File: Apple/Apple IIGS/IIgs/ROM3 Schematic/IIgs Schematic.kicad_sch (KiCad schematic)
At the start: 0 parts

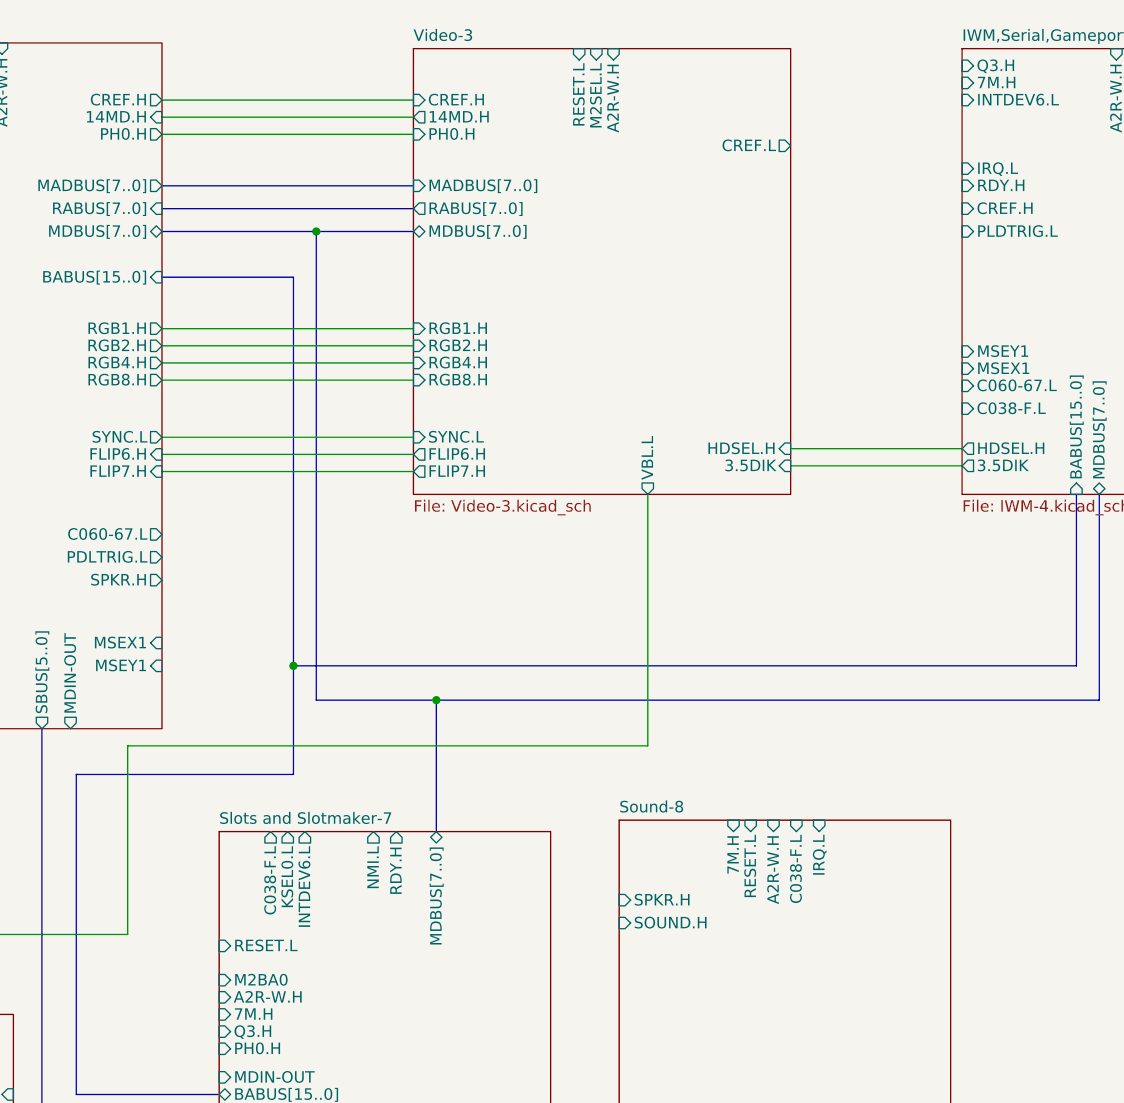
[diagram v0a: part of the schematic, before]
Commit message: 399 ERC, Rescue symbol clean-up
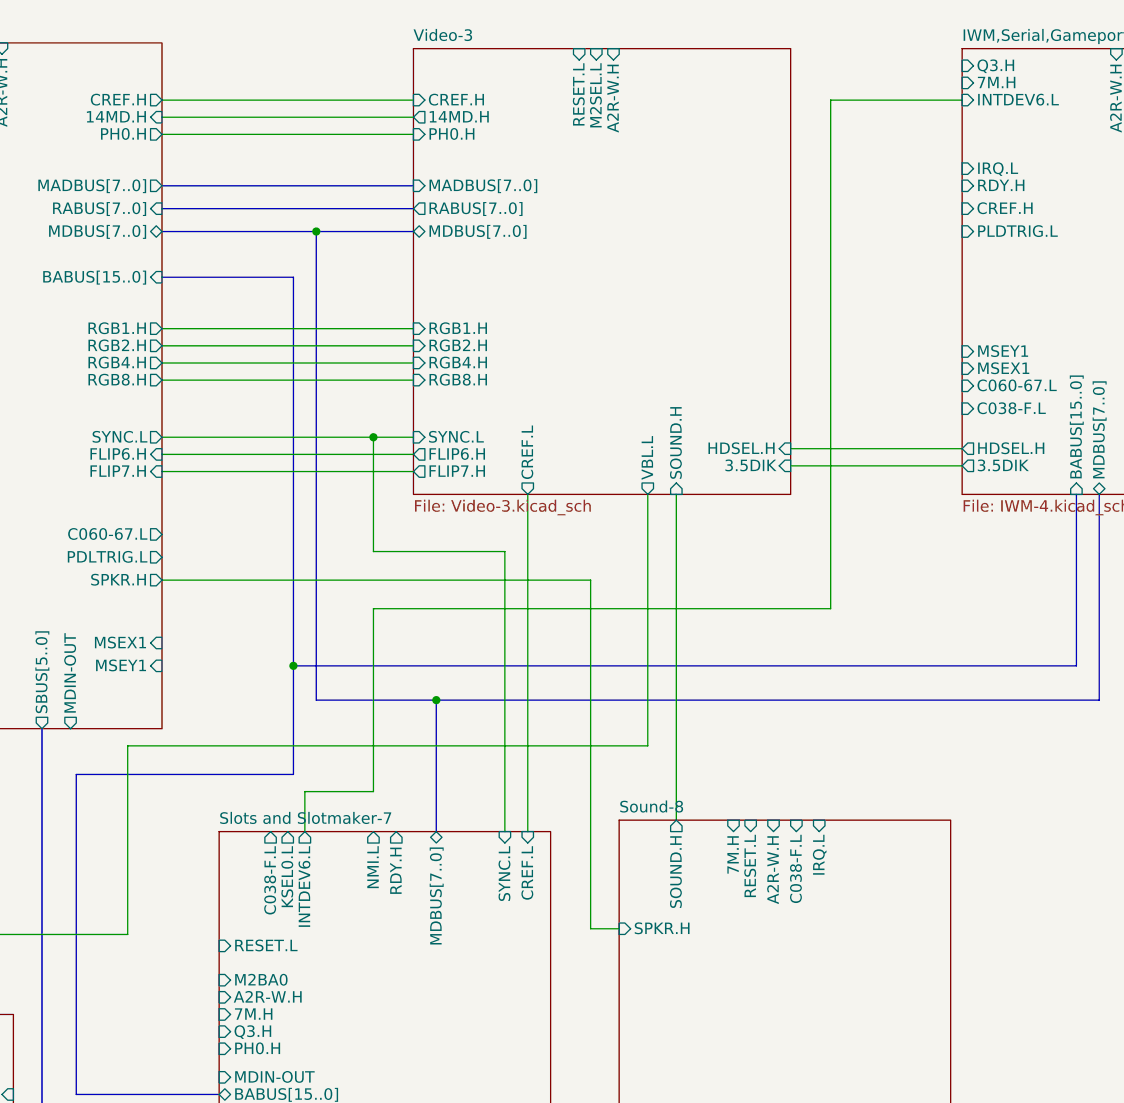
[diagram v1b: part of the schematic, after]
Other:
- sheet Slots and Slotmaker-7 ports: added CREF.L, SYNC.L; removed none
- sheet Video-3 ports: added SOUND.H; removed none

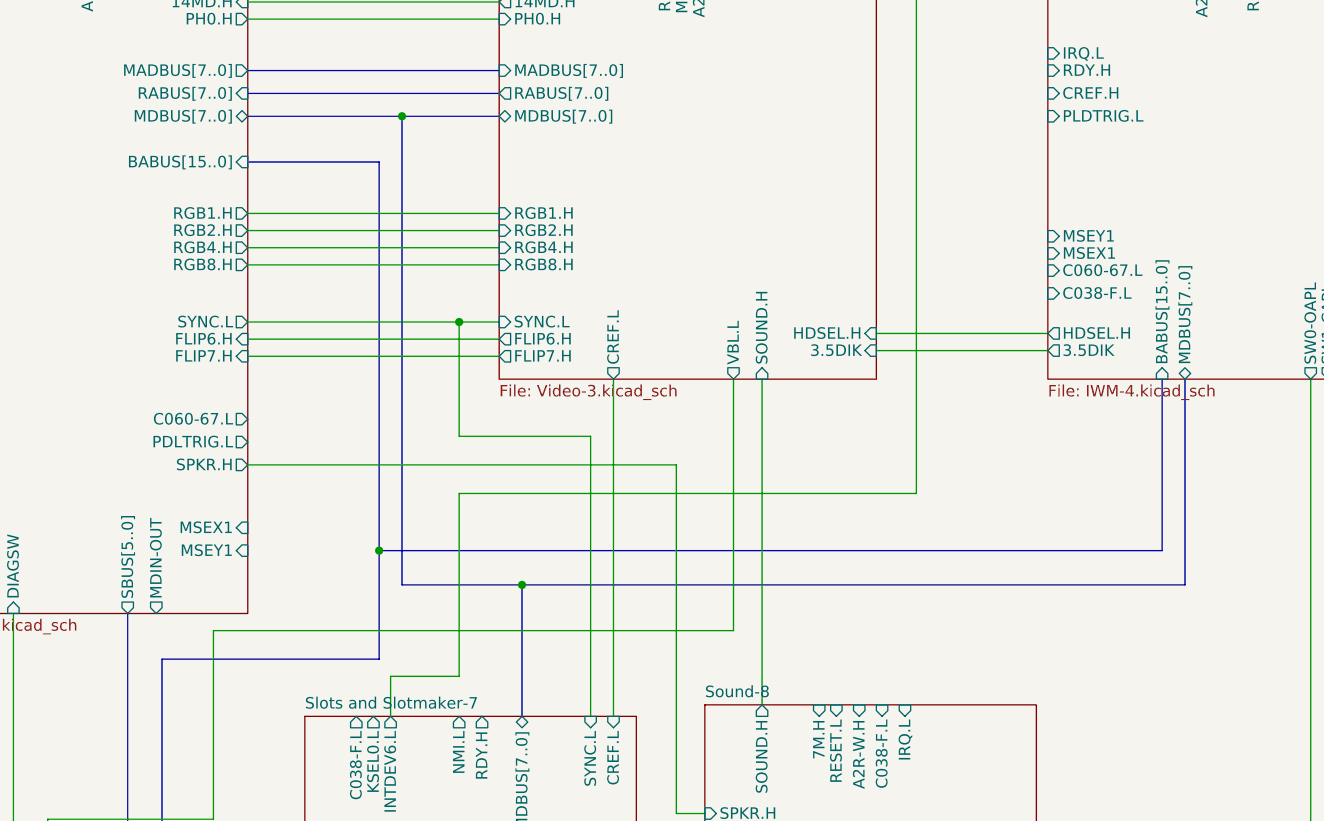
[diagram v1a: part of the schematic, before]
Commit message: moved v5 version to separate directory
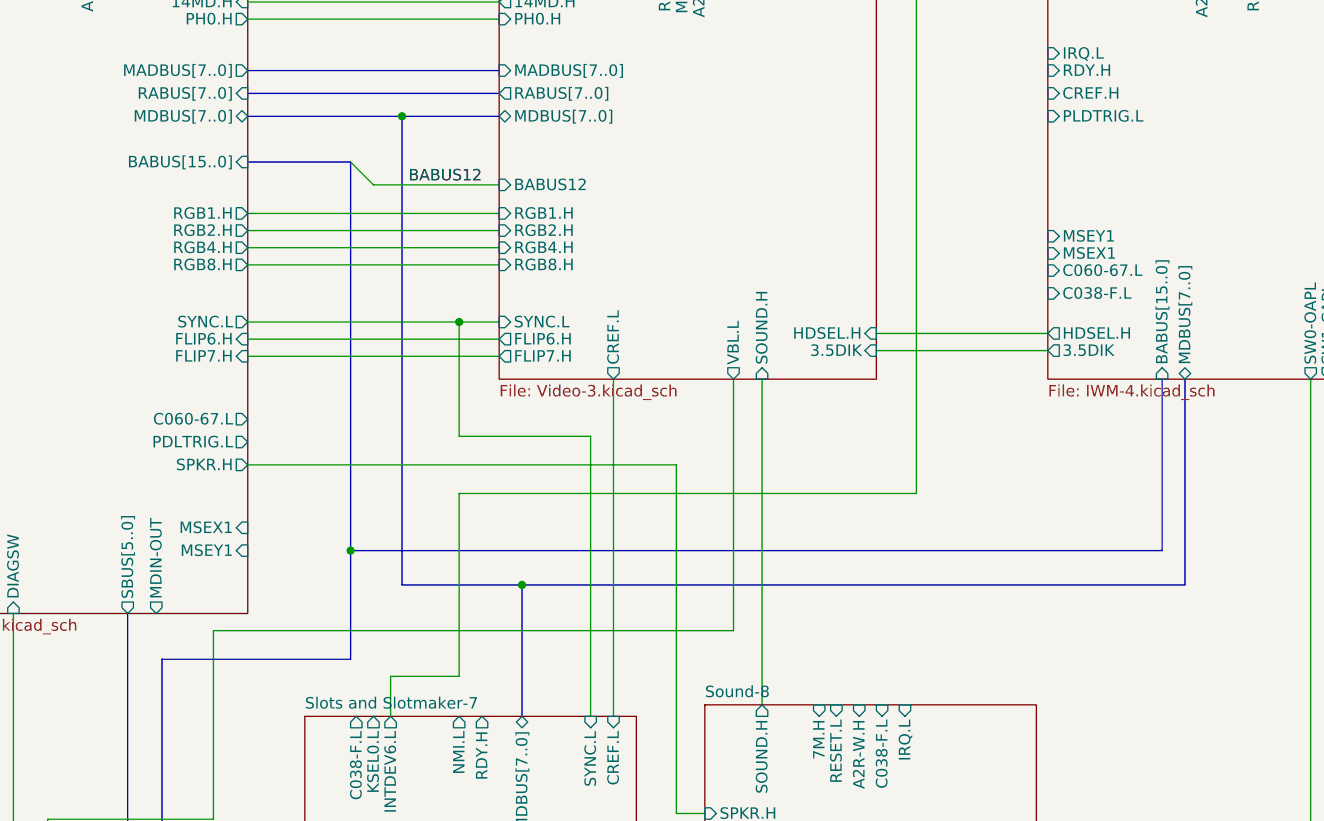
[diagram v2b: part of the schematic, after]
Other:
- sheet Video-3 ports: added BABUS12; removed none
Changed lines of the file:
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@@
   (junction (at 220.98 91.44) (diameter 0) (color 0 0 0 0)
   )
-  (junction (at 212.09 116.84) (diameter 0) (color 0 0 0 0)
+  (junction (at 208.915 116.84) (diameter 0) (color 0 0 0 0)
   )
   (junction (at 332.74 55.245) (diameter 0) (color 0 0 0 0)
   )
+  (bus_entry (at 208.915 73.66) (size 2.54 2.54)
+    (stroke (width 0) (type default) (color 0 0 0 0))
+  )
   (bus (pts (xy 214.63 68.58) (xy 225.425 68.58))
     (stroke (width 0) (type default) (color 0 0 0 0))
@@
     (stroke (width 0) (type default) (color 0 0 0 0))
   )
-  (bus (pts (xy 187.96 128.905) (xy 212.09 128.905))
+  (bus (pts (xy 208.915 116.84) (xy 299.085 116.84))
+    (stroke (width 0) (type default) (color 0 0 0 0))
+  )
+  (bus (pts (xy 187.96 128.905) (xy 208.915 128.905))
     (stroke (width 0) (type default) (color 0 0 0 0))
   )
@@
     (stroke (width 0) (type default) (color 0 0 0 0))
   )
+  (wire (pts (xy 211.455 76.2) (xy 225.425 76.2))
+    (stroke (width 0) (type default) (color 0 0 0 0))
+  )
   (bus (pts (xy 184.15 166.37) (xy 203.835 166.37))
     (stroke (width 0) (type default) (color 0 0 0 0))
@@
     (stroke (width 0) (type default) (color 0 0 0 0))
   )
-  (bus (pts (xy 212.09 116.84) (xy 212.09 128.905))
+  (bus (pts (xy 208.915 116.84) (xy 208.915 128.905))
     (stroke (width 0) (type default) (color 0 0 0 0))
   )
@@
     (stroke (width 0) (type default) (color 0 0 0 0))
   )
-  (bus (pts (xy 212.09 73.66) (xy 212.09 116.84))
+  (bus (pts (xy 208.915 73.66) (xy 208.915 116.84))
     (stroke (width 0) (type default) (color 0 0 0 0))
   )
@@
     (stroke (width 0) (type default) (color 0 0 0 0))
   )
-  (bus (pts (xy 212.09 116.84) (xy 299.085 116.84))
-    (stroke (width 0) (type default) (color 0 0 0 0))
-  )
   (wire (pts (xy 335.28 210.82) (xy 180.975 210.82))
     (stroke (width 0) (type default) (color 0 0 0 0))
@@
     (stroke (width 0) (type default) (color 0 0 0 0))
   )
-  (bus (pts (xy 197.485 73.66) (xy 212.09 73.66))
+  (bus (pts (xy 197.485 73.66) (xy 208.915 73.66))
     (stroke (width 0) (type default) (color 0 0 0 0))
   )
@@
   (bus (pts (xy 299.085 116.84) (xy 299.085 97.79))
     (stroke (width 0) (type default) (color 0 0 0 0))
+  )
+  (label "BABUS12" (at 223.52 76.2 180)
+    (effects (font (size 1.27 1.27)) (justify right bottom))
   )
   (sheet (at 88.265 47.625) (size 46.355 53.34) (fields_autoplaced)
@@
       (effects (font (size 1.27 1.27)) (justify left))
     )
+    (pin "BABUS12" input (at 225.425 76.2 180)
+      (effects (font (size 1.27 1.27)) (justify left))
+    )

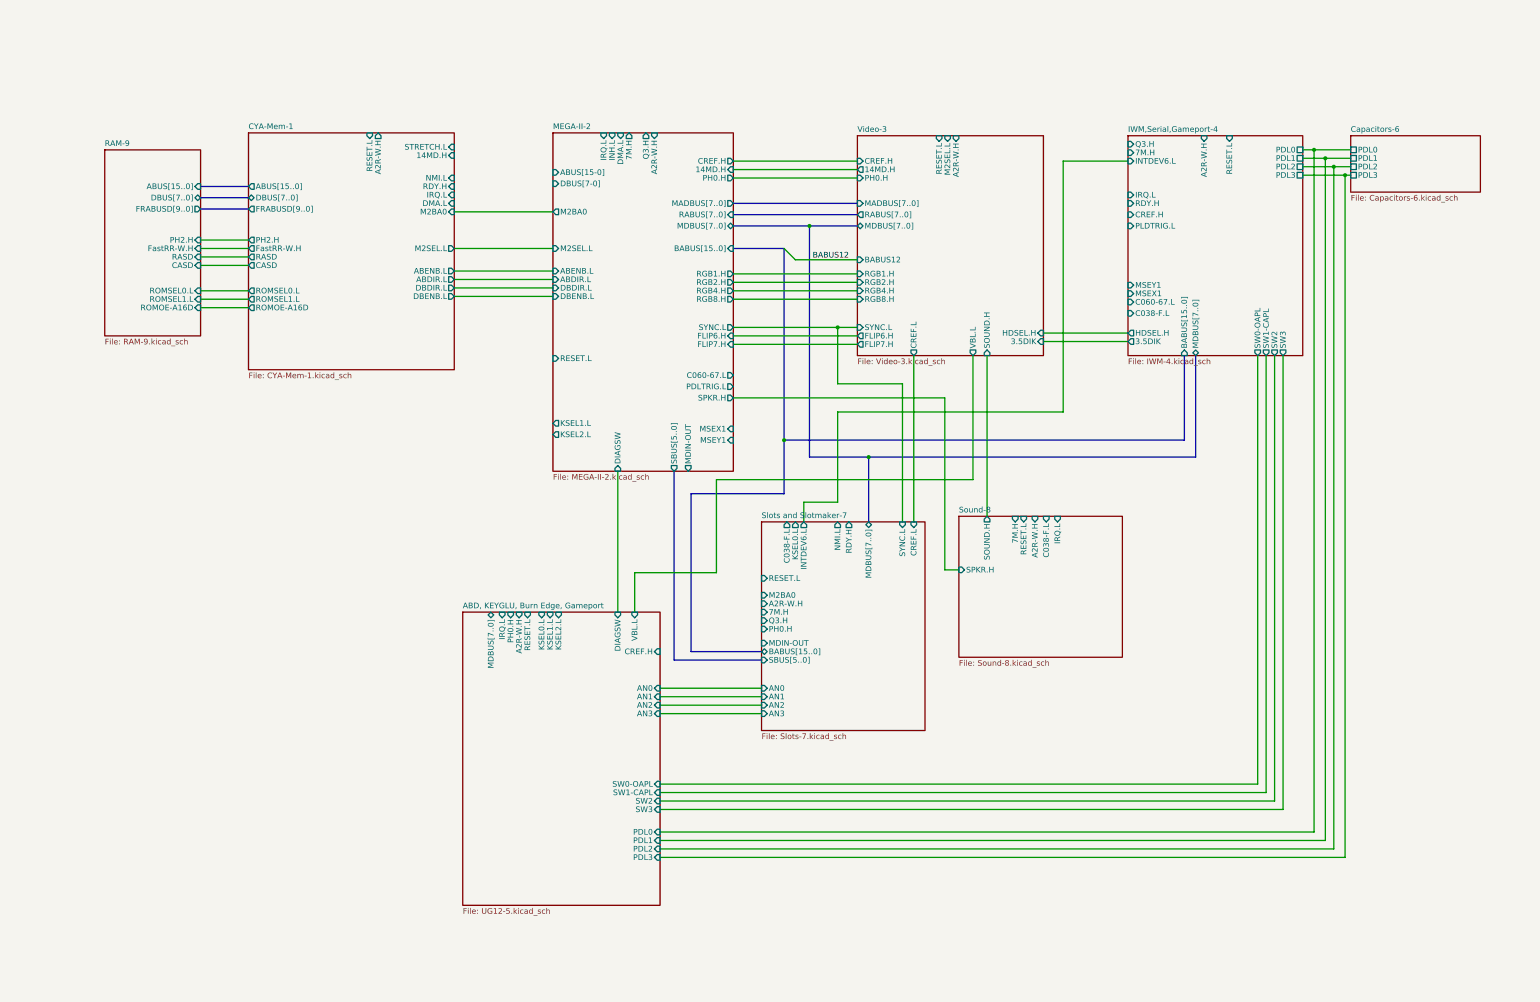
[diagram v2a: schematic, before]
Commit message: 0 ERC Errors AND Warnings. Whew. ICs updated with correct pin assignments and many (many) other fixes.
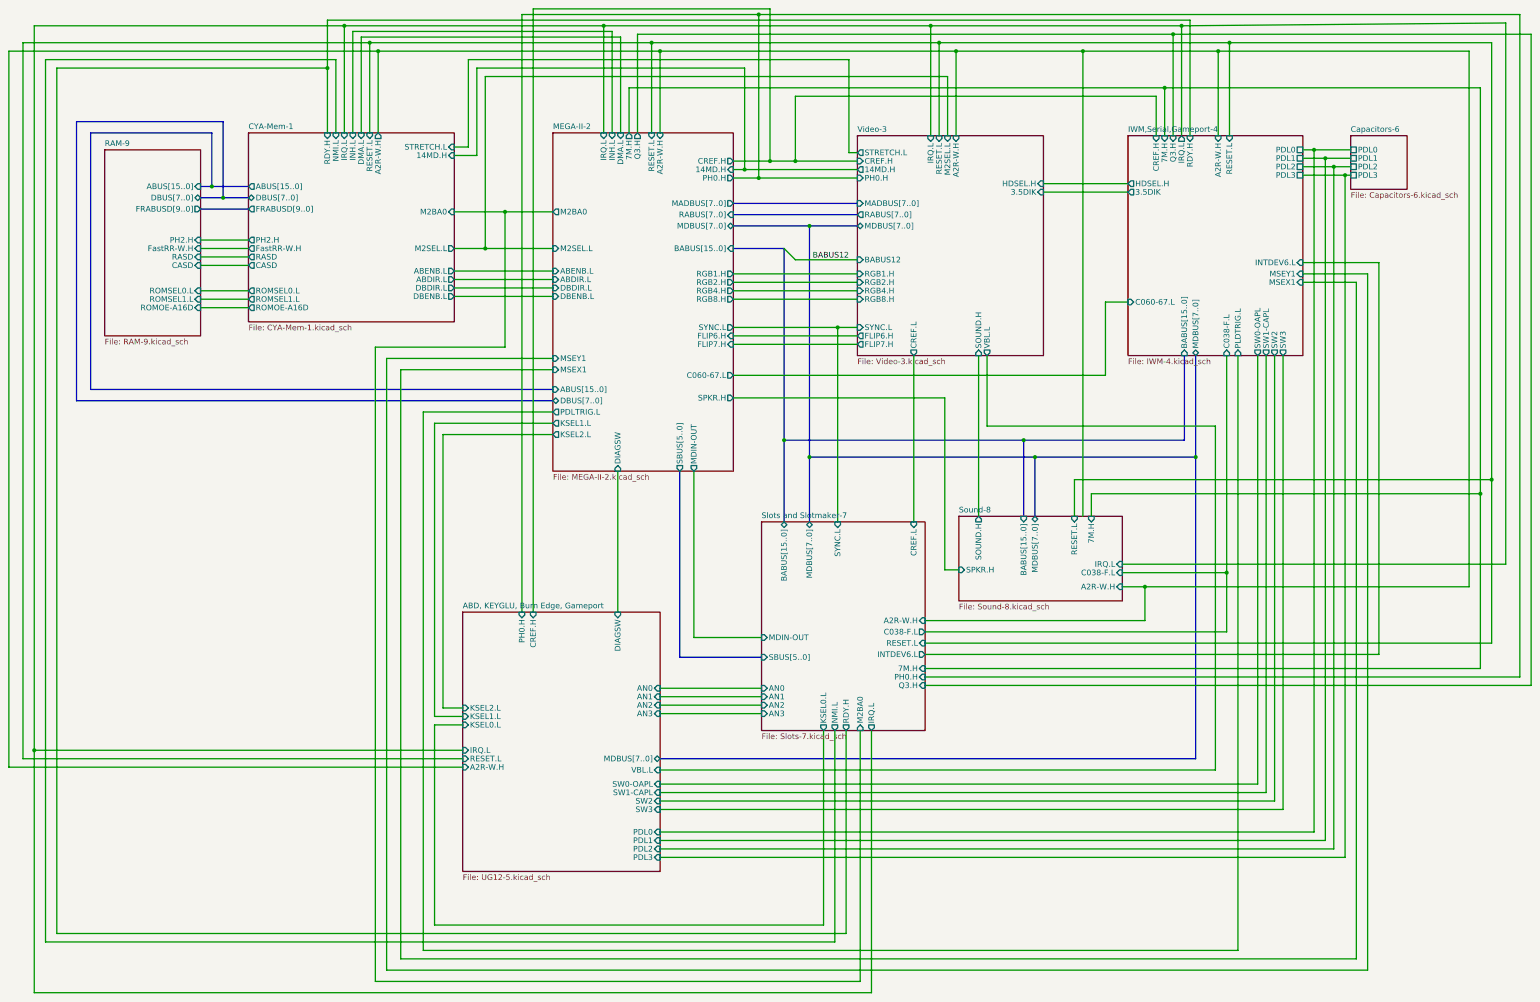
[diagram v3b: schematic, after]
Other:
- sheet CYA-Mem-1 ports: added INH.L; removed none
- sheet MEGA-II-2 ports: added ABUS[15..0], DBUS[7..0]; removed ABUS[15-0], DBUS[7-0]
- sheet Slots and Slotmaker-7 ports: added IRQ.L; removed none
- sheet Sound-8 ports: added BABUS[15..0], MDBUS[7..0]; removed none
- sheet Video-3 ports: added IRQ.L, STRETCH.L; removed none
